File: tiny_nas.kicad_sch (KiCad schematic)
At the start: 67 parts, among them SW1 SW_SPDT, U2 LAN8720A, Y1 16MHz

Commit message: complete first draft of schematics
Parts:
- removed J?: Micro_SD_Card_Det, symbol Connector:Micro_SD_Card_Det
- removed J?: HR911105A, HR911105A:HANRUN_HR911105A, symbol HR911105A:HR911105A
- removed R? (x12): 0R, symbol Device:R
- removed R?: 33R, symbol Device:R
- removed U?: USB3320C-EZK-TR, QFN50P500X500X100-33N330X330, symbol USB3320C-EZK-TR:USB3320C-EZK-TR
- added C22, C23: 10p, Capacitor_SMD:C_0402_1005Metric, symbol Device:C
- added C24, C25: 30p, Capacitor_SMD:C_0402_1005Metric, symbol Device:C
- added C26, C28, C31, C32, C33, C34, C37, C39, C40, C41, C42, C43, C44: 100n, Capacitor_SMD:C_0402_1005Metric, symbol Device:C
- added C27: 470p, Capacitor_SMD:C_0402_1005Metric, symbol Device:C
- added C29: 1u, Capacitor_SMD:C_0603_1608Metric, symbol Device:C
- added C30, C38: 4.7u, Capacitor_SMD:C_0603_1608Metric, symbol Device:C
- added C35: 10u, Capacitor_SMD:C_0805_2012Metric, symbol Device:C
- added FB1: 600R, Inductor_SMD:L_0603_1608Metric, symbol Device:FerriteBead
- added FB2: 120R, Inductor_SMD:L_0603_1608Metric, symbol Device:FerriteBead
- added J2: Micro_SD_Card_Det_Hirose_DM3AT, Connector_Card:microSD_HC_Hirose_DM3AT-SF-PEJM5, symbol Connector:Micro_SD_Card_Det_Hirose_DM3AT
- added J4, J8, J9: Conn_01x02_Male, Connector_PinHeader_2.54mm:PinHeader_1x02_P2.54mm_Vertical, symbol Connector:Conn_01x02_Male
- added J5: HR911105A, HR911105A:HANRUN_HR911105A, symbol HR911105A:HR911105A
- added JP1, JP2: SolderJumper_2_Bridged, Jumper:SolderJumper-2_P1.3mm_Bridged2Bar_RoundedPad1.0x1.5mm, symbol Jumper:SolderJumper_2_Bridged
- added R10, R11, R12, R13: 33R, Resistor_SMD:R_0402_1005Metric, symbol Device:R
- added R14, R33: 0R, Resistor_SMD:R_0402_1005Metric, symbol Device:R
- added R15, R16, R17, R18, R20: 47k, Resistor_SMD:R_0402_1005Metric, symbol Device:R
- added R21: 12.1k, Resistor_SMD:R_0402_1005Metric, symbol Device:R
- added R22, R24, R25, R28: 50R, Resistor_SMD:R_0402_1005Metric, symbol Device:R
- added R23, R4, R5, R6, R8, R9: 10k, Resistor_SMD:R_0402_1005Metric, symbol Device:R
- added R26, R27: 270R, Resistor_SMD:R_0402_1005Metric, symbol Device:R
- added R29: 12k, Resistor_SMD:R_0402_1005Metric, symbol Device:R
- added R7: 1k5, Resistor_SMD:R_0402_1005Metric, symbol Device:R
- added U4: USBLC6-4SC6, Package_TO_SOT_SMD:SOT-23-6, symbol Power_Protection:USBLC6-4SC6
- added Y2: 25MHz, Crystal:Crystal_SMD_HC49-SD, symbol Device:Crystal
- C1, C10, C11, C13, C4, C6, C7, C8, C9: footprint (none) -> Capacitor_SMD:C_0402_1005Metric
- C12: value C -> 100n; footprint (none) -> Capacitor_SMD:C_0402_1005Metric
- C14, C17: renamed from C?; value C -> 22u; footprint (none) -> Capacitor_SMD:C_0805_2012Metric
- C15, C16, C18, C19, C20, C21, C45, C46, C49, C50: renamed from C?; footprint (none) -> Capacitor_SMD:C_0402_1005Metric
- C2, C3, C5: footprint (none) -> Capacitor_SMD:C_0603_1608Metric
- C36: renamed from C?; value 100nF -> 100n; footprint (none) -> Capacitor_SMD:C_0402_1005Metric
- C47, C48: renamed from C?; value 4.7uF -> 4.7u; footprint (none) -> Capacitor_SMD:C_0603_1608Metric
- D1, D2: renamed from D?; footprint (none) -> LED_SMD:LED_0603_1608Metric
- FB3: renamed from FB?; footprint (none) -> Inductor_SMD:L_0603_1608Metric
- J1: renamed from J?; footprint (none) -> Connector_PinHeader_1.27mm:PinHeader_2x07_P1.27mm_Vertical
- J3, J6, J7: renamed from J?; footprint (none) -> Connector_USB:USB_Micro-B_Molex_47346-0001
- R1: footprint (none) -> Resistor_SMD:R_0402_1005Metric
- R19, R3, R30, R31, R32: renamed from R?; footprint (none) -> Resistor_SMD:R_0402_1005Metric
- R2: renamed from R?; value 1k -> 1k5; footprint (none) -> Resistor_SMD:R_0402_1005Metric
- SW1: footprint (none) -> Button_Switch_SMD:SW_SPDT_PCM12
- U6: renamed from U?; footprint SOP50P490X110-10N -> MAX1823BEUB:SOP50P490X110-10N
- Y1: footprint (none) -> Crystal:Crystal_SMD_3225-4Pin_3.2x2.5mm
- Y3: renamed from Y?; footprint (none) -> Crystal:Crystal_SMD_HC49-SD
- gave numbers to parts that had none: 4
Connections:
- net +3.3V is gone; now on net +3V3: U3.143 (PDR_ON)
- net +3V3: now also C10.1, C11.1, C15.1, C16.1, C18.1, C19.1, C2.1, C20.1, C21.1, C4.1, C6.1, C7.1, C8.1, C9.1, U2.9 (VDDIO), U3.108 (VDD), U3.121 (VDD), U3.131 (VDD), U3.144 (VDD), U3.17 (VDD), U3.30 (VDD), U3.39 (VDD), U3.52 (VDD), U3.6 (VBAT), U3.62 (VDD), U3.72 (VDD), U3.84 (VDD), U3.95 (VDD), U5.16 (VDD3.3), U5.25 (VDD3.3), U5.30 (VDD3.3), U5.6 (VDD3.3), C26.1, C33.1, C37.1, C39.1, C40.1, FB1.1, J2.4 (VDD), R15.1, R16.1, R17.1, R18.1, R20.1, R33.2, R4.2, R5.2, R6.2, R7.2, R8.2
- net GND: now also U2.25 (VSS), U5.1 (GND), U5.2 (GND), U5.33 (GND), C22.2, C23.2, C24.2, C25.2, C26.2, C27.1, C28.2, C29.1, C30.2, C31.2, C32.2, C33.2, C34.2, C35.2, C37.2, C38.2, C39.2, C40.2, C41.2, C42.2, C43.2, C44.2, J2.6 (VSS), J4.2 (Pin_2), J5.15 (SHIELD), J5.16 (SHIELD), J5.8, J8.1 (Pin_1), J9.1 (Pin_1), R21.2, R23.2, R26.1, R27.1, R29.2, R9.2, U4.2 (GND); no longer J3.5 (GND), J6.5 (GND)
- net ULPI_D6: now reaches U3.74 (PB13)
- net ULPI_D6: now also U5.18 (DATA6)
- net ULPI_D2: now reaches U3.47 (PB1)
- net ULPI_D2: now also U5.22 (DATA2)
- net ULPI_NXT: now reaches U5.11 (NXT)
- net ULPI_NXT: now also U3.29 (PC3)
- net ULPI_DIR: now reaches U5.12 (DIR)
- net ULPI_DIR: now also U3.28 (PC2)
- net ULPI_STP: now reaches U5.13 (STP)
- net ULPI_STP: now also U3.26 (PC0)
- net ULPI_CK: now reaches U5.14 (CLKOUT)
- net ULPI_CK: now also U3.41 (PA5)
- net at U5.15 (VDD1.8): now also JP2.2 (B)
- net ULPI_D7: now reaches U5.17 (DATA7)
- net ULPI_D7: now also U3.135 (PB5)
- net ULPI_D5: now reaches U5.19 (DATA5)
- net ULPI_D5: now also U3.73 (PB12)
- net ULPI_D4: now reaches U5.20 (DATA4)
- net ULPI_D4: now also U3.70 (PB11)
- net ULPI_D3: now reaches U5.21 (DATA3)
- net ULPI_D3: now also U3.69 (PB10)
- net ULPI_D1: now reaches U5.23 (DATA1)
- net ULPI_D1: now also U3.46 (PB0)
- net ULPI_D0: now reaches U5.24 (DATA0)
- net ULPI_D0: now also U3.37 (PA3)
- net at U5.26 (VDD1.8): now also JP1.2 (B)
- net at U5.29 (VDDA1.8): now also C34.1, C38.1
- net at U5.31 (REG_EN): now also R33.1
- net at U5.32 (RBIAS): now also R29.1
- net at J6.4 (ID), U5.5 (ID): now also J4.1 (Pin_1)
- net ULPI_RESET: now reaches U5.9 (RESET)
- net ULPI_RESET: now also U3.97 (PC7)
- net at U3.111 (PC10): now also J2.1 (DAT2), R15.2
- net at U3.112 (PC11): now also J2.2 (DAT3/CD), R16.2
- net at U3.116 (PD2): now also J2.3 (CMD), R17.2
- net at U3.113 (PC12): now also J2.5 (CLK)
- net at U3.98 (PC8): now also J2.7 (DAT0), R18.2
- net at U3.99 (PC9): now also J2.8 (DAT1), R20.2
- net RCC_OSC_IN: now reaches U3.23 (PH0), Y1.1
- net RCC_OSC_IN: now also C22.1
- net RCC_OSC_OUT: now reaches U3.24 (PH1), Y1.3
- net RCC_OSC_OUT: now also C23.1
- net at C12.2, J1.12 (Pin_12), U3.25 (NRST): now also U2.15 (RST)
- net USART_RX: now reaches J1.13 (Pin_13), U3.102 (PA10), U7.8 (TXD)
- net USART_TX: now reaches J1.14 (Pin_14), U3.101 (PA9), U7.9 (RXD)
- net at C48.1, U6.9 (OUTA): now also FB2.1
- net at J3.1 (VBUS): now also FB2.2
- net USB_FS_DP: now reaches J3.3 (D+), U3.104 (PA12)
- net at J3.4 (ID): no longer U3.87 (PG2)
- net at U2.1 (VDD2A): now also U2.19 (VDD1A), C31.1, C32.1, C35.1, C41.1, C42.1, C43.1, C44.1, FB1.2, J5.4, J5.5, R22.1, R24.1, R25.1, R28.1, U4.5 (VBUS)
- net at U2.10 (RXER/PHYAD0): now also R9.1
- net at U3.43 (PA7): now also R11.1; no longer U2.11 (CRS_DV/MODE2)
- net at U2.12 (MDIO): now also R14.2, R7.1; no longer U3.36 (PA2)
- net at U3.35 (PA1): now also R10.1; no longer U2.14 (INT/REFCLKO)
- net at U2.2 (LED2/nINTSEL): now also J5.12, R23.1
- net at U2.20 (TXN): now also J5.2, R25.2, U4.4 (I/O3)
- net at U2.21 (TXP): now also J5.1, R28.2, U4.3 (I/O2)
- net at U2.22 (RXN): now also J5.6, R22.2, U4.6 (I/O4)
- net at U2.23 (RXP): now also J5.3, R24.2, U4.1 (I/O1)
- net at U2.24 (RBIAS): now also R21.1
- net at U2.3 (LED1/REGOFF): now also J5.9
- net at U2.4 (XTAL2): now also C25.1, Y2.2
- net at U2.5 (XTAL1/CLKIN): now also C24.1, Y2.1
- net at U2.6 (VDDCR): now also C27.2, C29.2
- net at U2.7 (RXD1/MODE1): now also R13.2, R5.1; no longer U3.45 (PC5)
- net at U3.44 (PC4): now also R12.1; no longer U2.8 (RXD0/MODE0)
- net at U3.114 (PD0): now also J2.10 (DET_A)
- net at U3.115 (PD1): now also J2.9 (DET_B)
- new net: R11.2, R6.1, U2.11 (CRS_DV/MODE2)
- new net: J5.11, R26.2
- new net: J6.5 (GND), J9.2 (Pin_2)
- new net: C28.1, C30.1, JP1.1 (A), JP2.1 (A)
- new net: R12.2, R4.1, U2.8 (RXD0/MODE0)
- new net: R10.2, R8.1, U2.14 (INT/REFCLKO)
- new net: J3.5 (GND), J8.2 (Pin_2)
- new net: J5.10, R27.2
- new net: R14.1, U3.36 (PA2)
- new net: R13.1, U3.45 (PC5)
- no-connect marks 11 -> 85
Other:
- moved on the sheet: C10, C11, C15, C16, C18, C19, C2, C20, C21, C4, C6, C7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

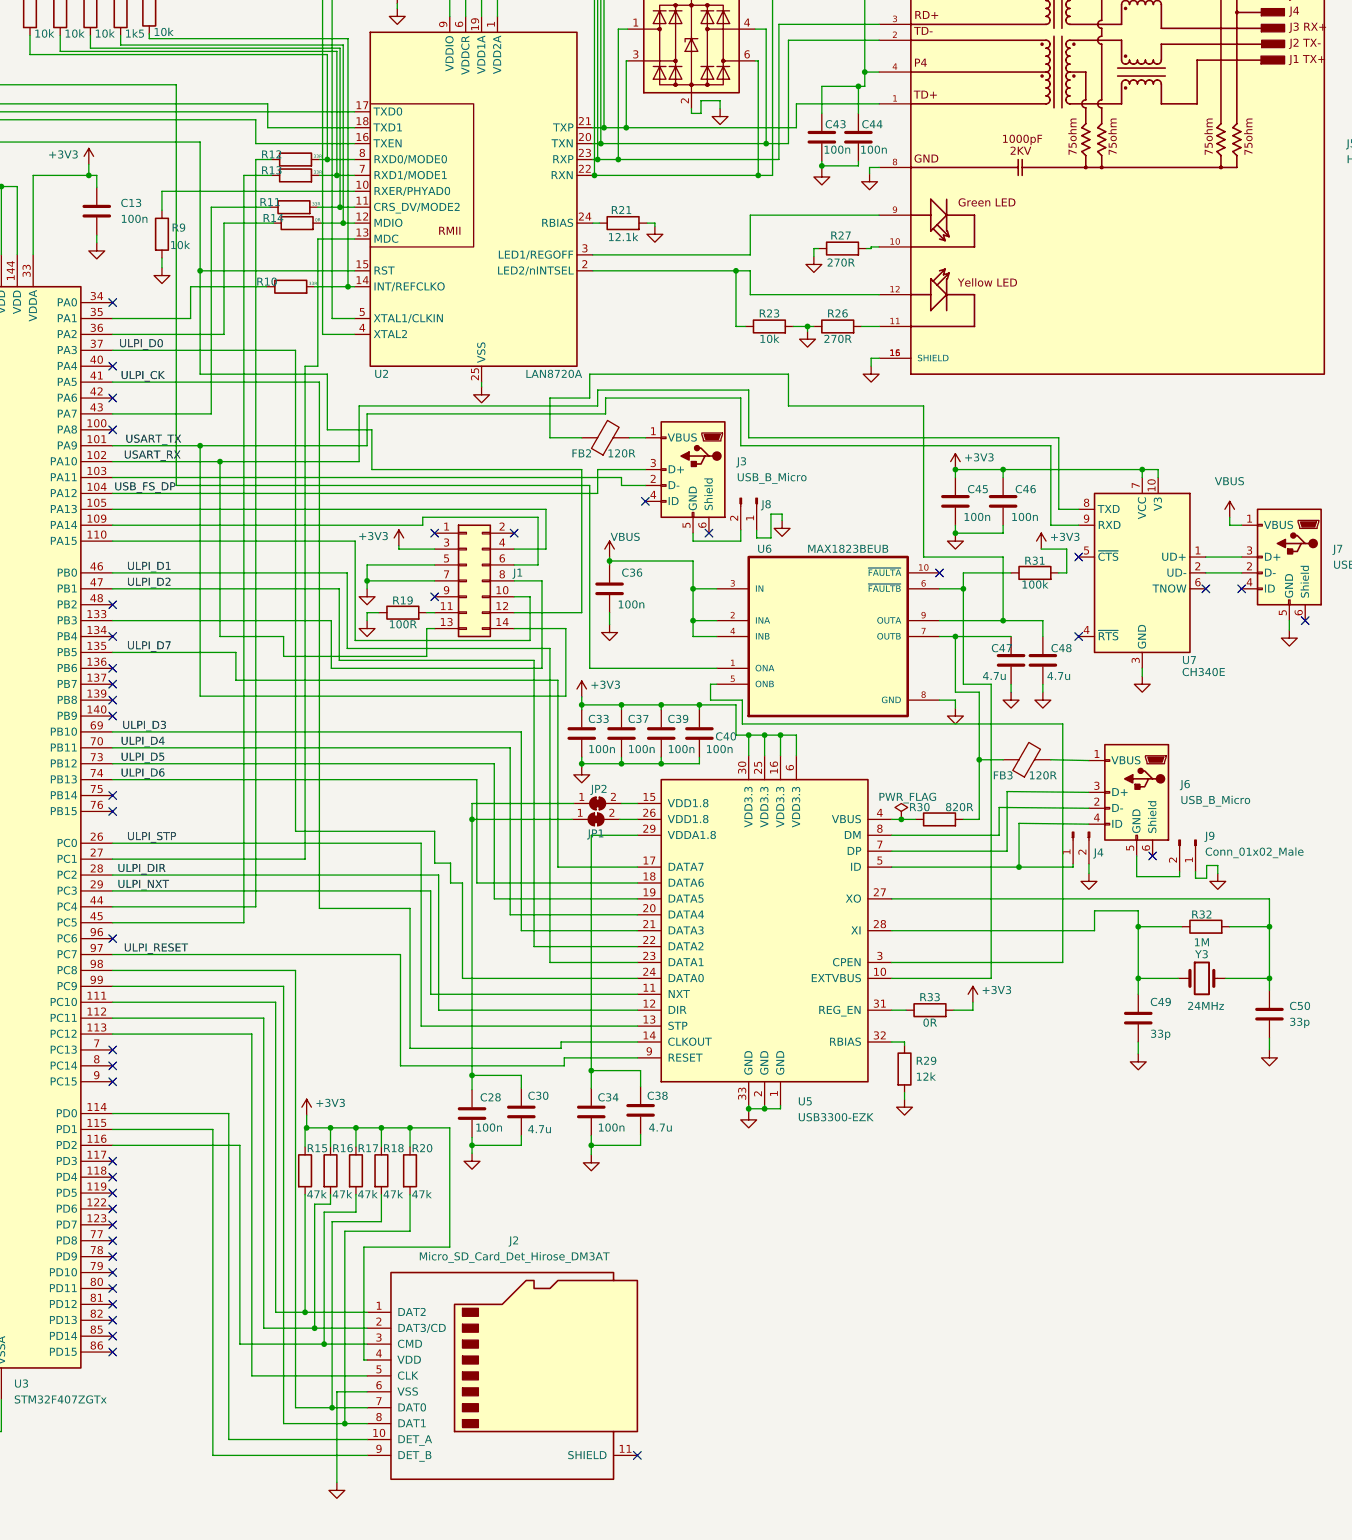
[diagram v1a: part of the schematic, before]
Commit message: pcb component placement
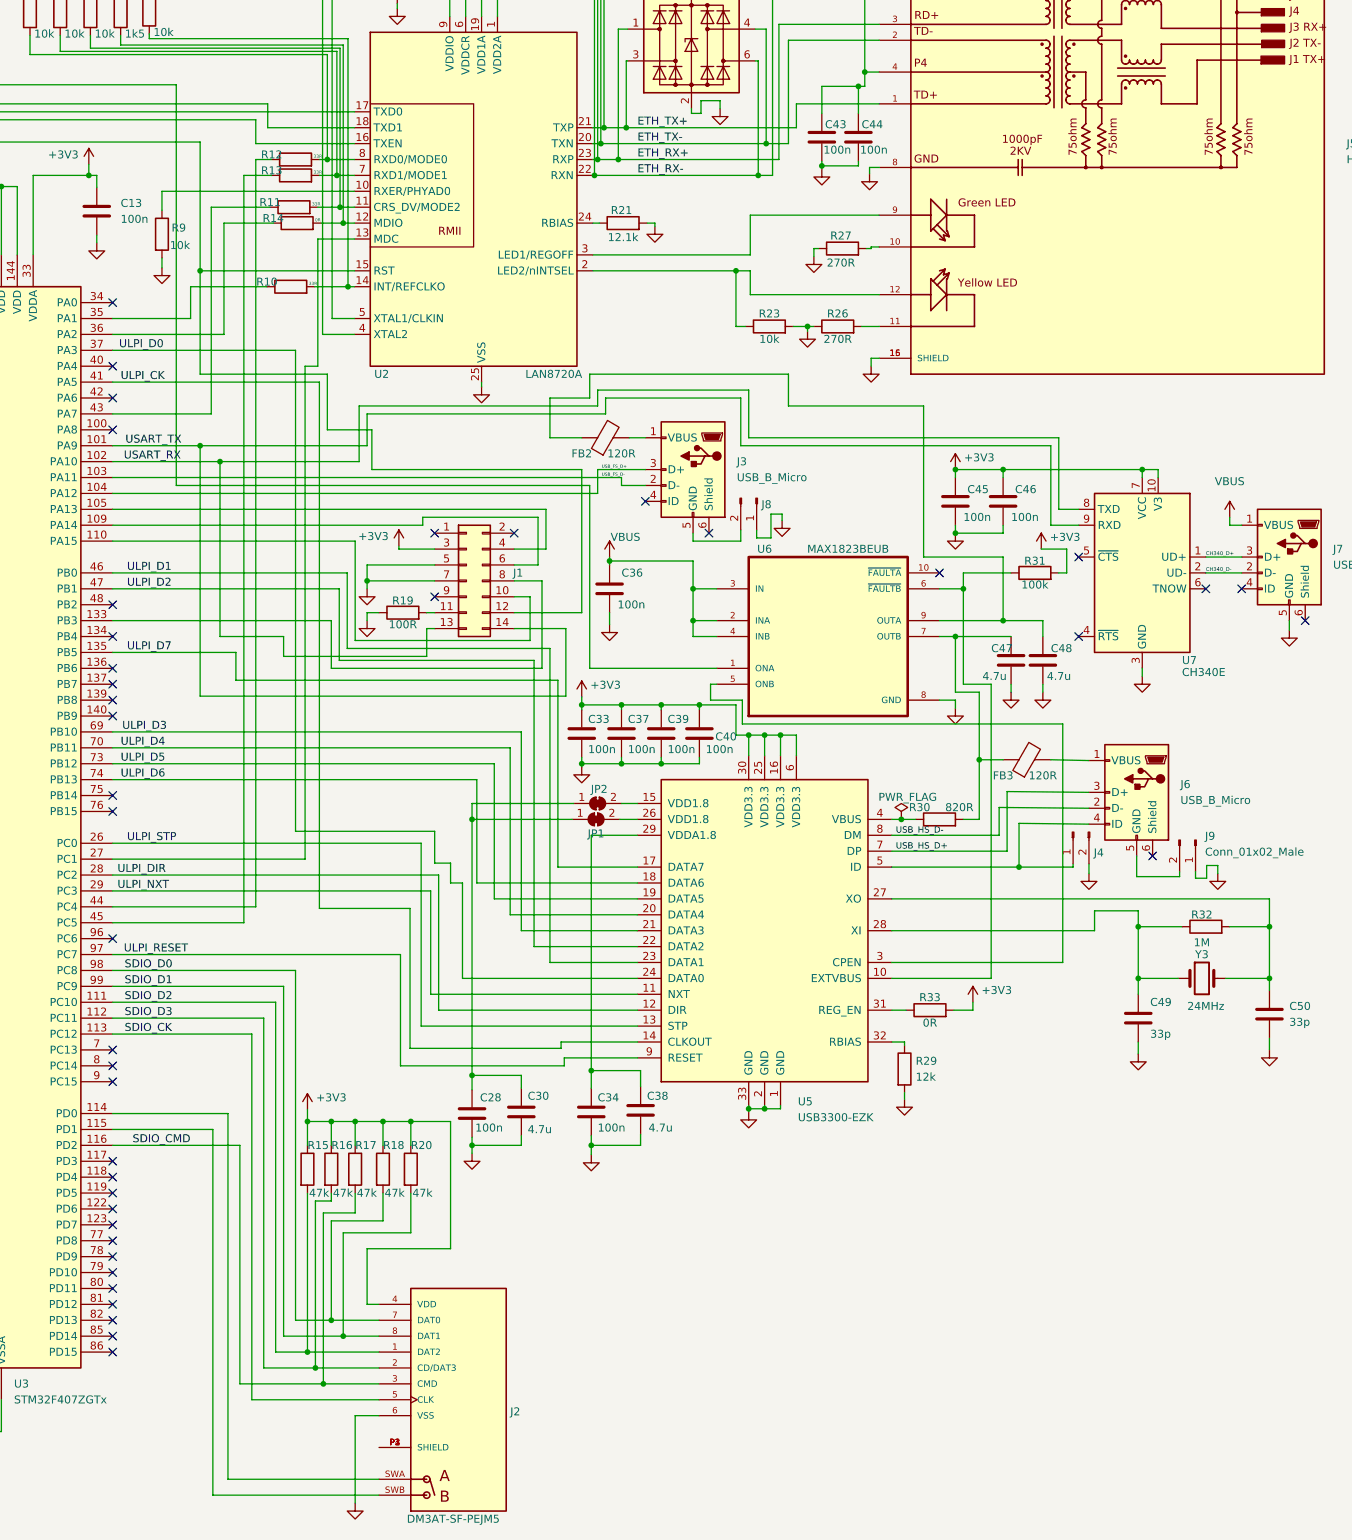
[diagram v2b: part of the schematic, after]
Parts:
- removed J2: Micro_SD_Card_Det_Hirose_DM3AT, Connector_Card:microSD_HC_Hirose_DM3AT-SF-PEJM5, symbol Connector:Micro_SD_Card_Det_Hirose_DM3AT
- added J2: DM3AT-SF-PEJM5, DM3AT-SF-PEJM5:HRS_DM3AT-SF-PEJM5, symbol DM3AT-SF-PEJM5:DM3AT-SF-PEJM5
- JP1, JP2: footprint Jumper:SolderJumper-2_P1.3mm_Bridged2Bar_RoundedPad1.0x1.5mm -> Jumper:SolderJumper-2_P1.3mm_Bridged_RoundedPad1.0x1.5mm
- U6: footprint MAX1823BEUB:SOP50P490X110-10N -> MAX1823BEUB_T:SOP50P490X110-10N
- Y2, Y3: footprint Crystal:Crystal_SMD_HC49-SD -> Crystal:Crystal_HC49-U_Vertical
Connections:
- net +3V3: now also J2.4 (VDD)
- net GND: now also J2.6 (VSS)
- net ETH_RX-: now reaches J5.6, R22.2, U2.22 (RXN), U4.6 (I/O4)
- net SDIO_D0: now reaches R18.2, U3.98 (PC8)
- net SDIO_D0: now also J2.7 (DAT0)
- net USB_HS_D+: now reaches J6.3 (D+), U5.7 (DP)
- net USB_HS_D-: now reaches J6.2 (D-), U5.8 (DM)
- net ETH_TX+: now reaches J5.1, R28.2, U2.21 (TXP), U4.3 (I/O2)
- net CH340_D-: now reaches J7.2 (D-), U7.2 (UD-)
- net CH340_D+: now reaches J7.3 (D+), U7.1 (UD+)
- net ETH_RX+: now reaches J5.3, R24.2, U2.23 (RXP), U4.1 (I/O1)
- net ETH_TX-: now reaches J5.2, R25.2, U2.20 (TXN), U4.4 (I/O3)
- net SDIO_CMD: now reaches R17.2, U3.116 (PD2)
- net SDIO_CMD: now also J2.3 (CMD)
- net SDIO_D3: now reaches R16.2, U3.112 (PC11)
- net SDIO_D3: now also J2.2 (CD/DAT3)
- net USB_FS_D-: now reaches J3.2 (D-), U3.103 (PA11)
- net SDIO_D2: now reaches R15.2, U3.111 (PC10)
- net SDIO_D2: now also J2.1 (DAT2)
- net SDIO_D1: now reaches R20.2, U3.99 (PC9)
- net SDIO_D1: now also J2.8 (DAT1)
- net at U3.114 (PD0): now also J2.SWA
- net SDIO_CK: now reaches U3.113 (PC12)
- net SDIO_CK: now also J2.5 (CLK)
- net at U3.115 (PD1): now also J2.SWB
- net USB_FS_DP renamed USB_FS_D+
- new net: J2.P1 (SHIELD), J2.P2 (SHIELD), J2.P3 (SHIELD), J2.P4 (SHIELD)
- no-connect marks 85 -> 84
